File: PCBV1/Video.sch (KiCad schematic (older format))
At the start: 0 parts

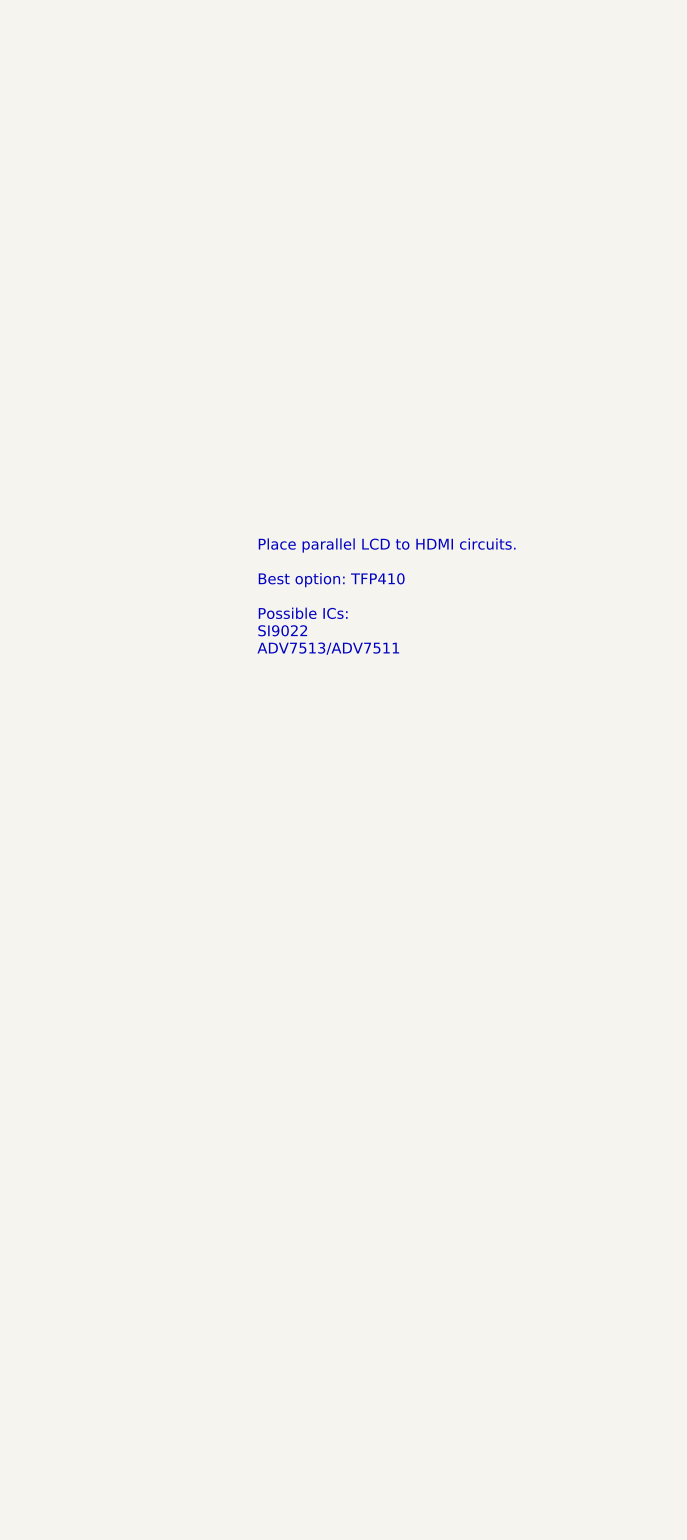
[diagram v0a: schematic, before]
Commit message: Merge of recent changes to default master (#2)
* Made a bunch of very small changes.

* Added UART, modifications to video etc.

* Minor adjustments with video connections.

* Finished video signals, added HDMI and SD connectors.
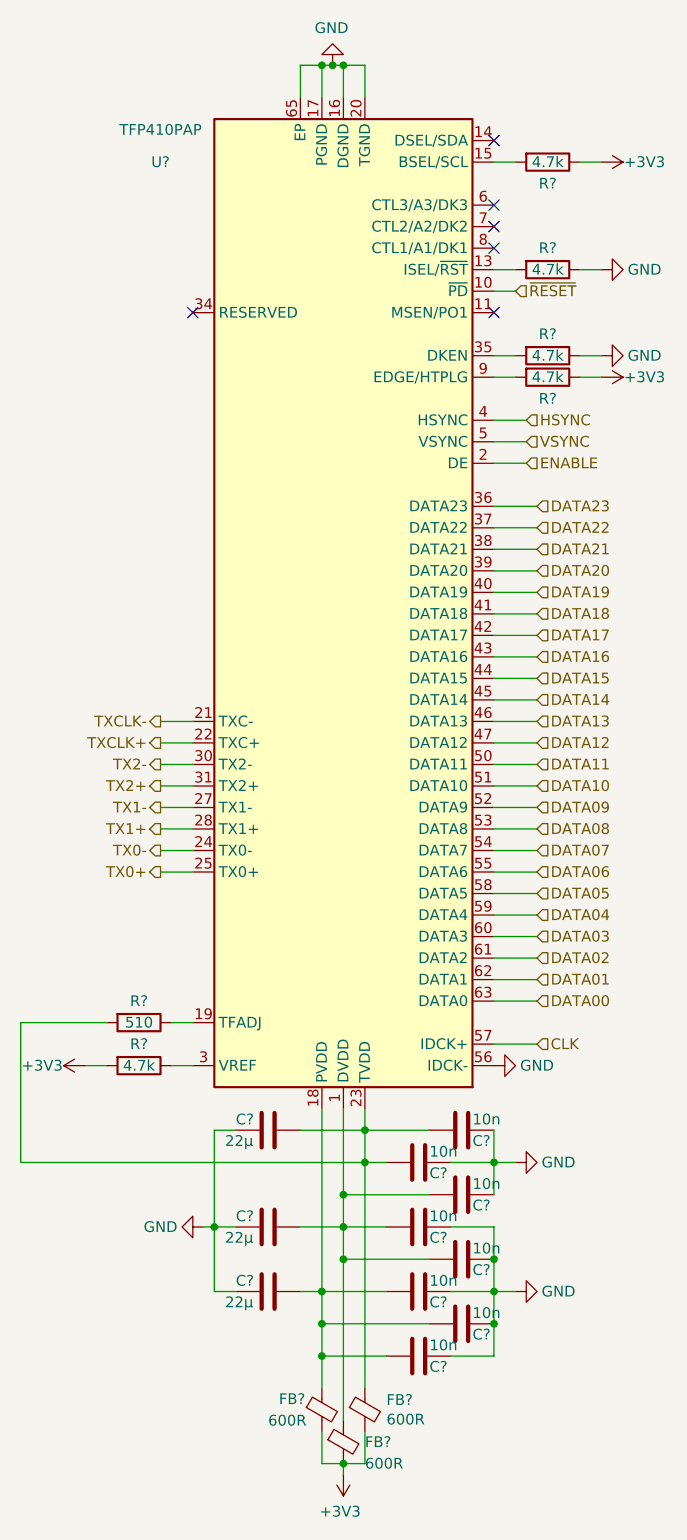
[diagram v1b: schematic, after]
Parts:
- added C? (x3): 22µ, Capacitor_SMD:C_0603_1608Metric, symbol Device:C
- added C? (x8): 10n, Capacitor_SMD:C_0603_1608Metric, symbol Device:C
- added FB? (x3): 600R, Inductor_SMD:L_0603_1608Metric, symbol Device:Ferrite_Bead_Small
- added R? (x5): 4.7k, Resistor_SMD:R_0603_1608Metric, symbol Device:R
- added R?: 510, Resistor_SMD:R_0603_1608Metric, symbol Device:R
- added U?: TFP410PAP, Package_QFP:HTQFP-64-1EP_10x10mm_P0.5mm_EP8x8mm_Mask4.4x4.4mm_ThermalVias, symbol Video:TFP410PAP
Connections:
- new net: C?.1, C?.2, C?.2, C?.2, FB?.1, U?.1 (DVDD), U?.12 (DVDD), U?.33 (DVDD)
- new net: R?.2, U?.13 (ISEL/~RST)
- new net: R?.2, U?.15 (BSEL/SCL)
- new net: C?.1, C?.2, C?.2, C?.2, FB?.1, U?.18 (PVDD)
- new net: R?.1, U?.19 (TFADJ)
- new net: C?.1, C?.2, C?.2, FB?.1, R?.2, U?.23 (TVDD), U?.29 (TVDD)
- new net: R?.1, U?.3 (VREF)
- new net: R?.2, U?.35 (DKEN)
- new net: R?.2, U?.9 (EDGE/HTPLG)
- new net +3V3: FB?.2, FB?.2, FB?.2, R?.1, R?.1, R?.2
- new net CLK: U?.57 (IDCK+)
- new net DATA00: U?.63 (DATA0)
- new net DATA01: U?.62 (DATA1)
- new net DATA02: U?.61 (DATA2)
- new net DATA03: U?.60 (DATA3)
- new net DATA04: U?.59 (DATA4)
- new net DATA05: U?.58 (DATA5)
- new net DATA06: U?.55 (DATA6)
- new net DATA07: U?.54 (DATA7)
- new net DATA08: U?.53 (DATA8)
- new net DATA09: U?.52 (DATA9)
- new net DATA10: U?.51 (DATA10)
- new net DATA11: U?.50 (DATA11)
- new net DATA12: U?.47 (DATA12)
- new net DATA13: U?.46 (DATA13)
- new net DATA14: U?.45 (DATA14)
- new net DATA15: U?.44 (DATA15)
- new net DATA16: U?.43 (DATA16)
- new net DATA17: U?.42 (DATA17)
- new net DATA18: U?.41 (DATA18)
- new net DATA19: U?.40 (DATA19)
- new net DATA20: U?.39 (DATA20)
- new net DATA21: U?.38 (DATA21)
- new net DATA22: U?.37 (DATA22)
- new net DATA23: U?.36 (DATA23)
- new net ENABLE: U?.2 (DE)
- new net GND: C?.1, C?.1, C?.1, C?.1, C?.1, C?.1, C?.1, C?.1, C?.2, C?.2, C?.2, R?.1, R?.1, U?.16 (DGND), U?.17 (PGND), U?.20 (TGND), U?.26 (TGND), U?.32 (TGND), U?.48 (DGND), U?.56 (IDCK-), U?.64 (DGND), U?.65 (EP)
- new net HSYNC: U?.4 (HSYNC)
- new net TX0+: U?.25 (TX0+)
- new net TX0-: U?.24 (TX0-)
- new net TX1+: U?.28 (TX1+)
- new net TX1-: U?.27 (TX1-)
- new net TX2+: U?.31 (TX2+)
- new net TX2-: U?.30 (TX2-)
- new net TXCLK+: U?.22 (TXC+)
- new net TXCLK-: U?.21 (TXC-)
- new net VSYNC: U?.5 (VSYNC)
- new net ~RESET: U?.10 (~PD)
- no-connect marks 0 -> 6
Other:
- note removed: "Place parallel LCD to HDMI circuits. \n\nBest option: TFP410\n\nPossible ICs:\nSI9022\nADV7513/ADV7511"
